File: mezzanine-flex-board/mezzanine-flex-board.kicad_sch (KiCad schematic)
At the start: 2 parts, among them J1 Mezzanine Plug, J2 Mezzanine Plug

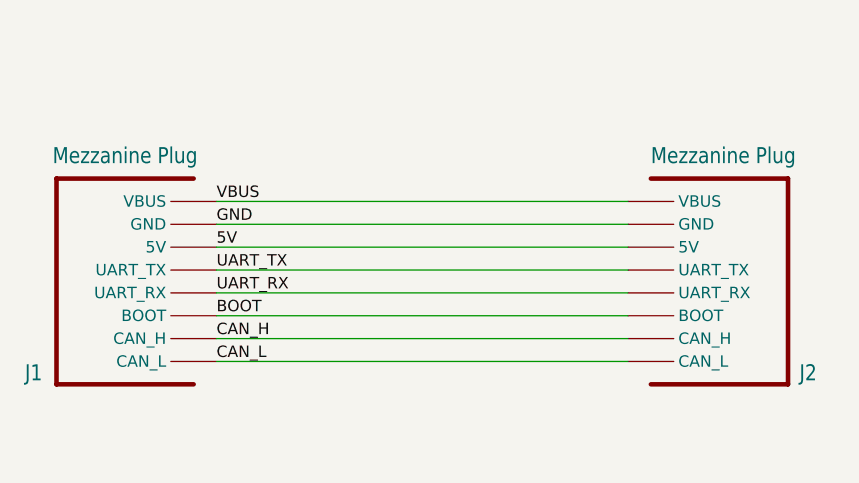
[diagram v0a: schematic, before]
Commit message: changed mezanine flex board to shorten to 14.5mm down from 19mm
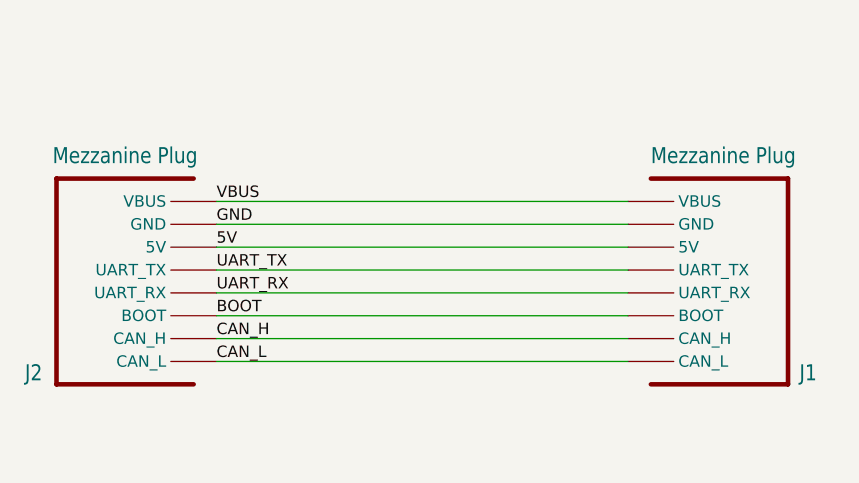
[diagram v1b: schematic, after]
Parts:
- renumbered J2 to J1, J1 to J2
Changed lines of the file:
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@@
-(kicad_sch (version 20211123) (generator eeschema)
+(kicad_sch (version 20230121) (generator eeschema)
   (paper "A4")
   (wire (pts (xy 114.3 101.6) (xy 160.02 101.6))
-    (stroke (width 0) (type default) (color 0 0 0 0))
+    (stroke (width 0) (type default))
   )
   (wire (pts (xy 114.3 99.06) (xy 160.02 99.06))
-    (stroke (width 0) (type default) (color 0 0 0 0))
+    (stroke (width 0) (type default))
   )
   (wire (pts (xy 114.3 96.52) (xy 160.02 96.52))
-    (stroke (width 0) (type default) (color 0 0 0 0))
+    (stroke (width 0) (type default))
   )
   (wire (pts (xy 114.3 91.44) (xy 160.02 91.44))
-    (stroke (width 0) (type default) (color 0 0 0 0))
+    (stroke (width 0) (type default))
   )
   (wire (pts (xy 114.3 104.14) (xy 160.02 104.14))
-    (stroke (width 0) (type default) (color 0 0 0 0))
+    (stroke (width 0) (type default))
   )
   (wire (pts (xy 114.3 88.9) (xy 160.02 88.9))
-    (stroke (width 0) (type default) (color 0 0 0 0))
+    (stroke (width 0) (type default))
   )
   (wire (pts (xy 114.3 86.36) (xy 160.02 86.36))
-    (stroke (width 0) (type default) (color 0 0 0 0))
+    (stroke (width 0) (type default))
   )
   (wire (pts (xy 114.3 93.98) (xy 160.02 93.98))
-    (stroke (width 0) (type default) (color 0 0 0 0))
+    (stroke (width 0) (type default))
   )
-  (label "BOOT" (at 114.3 99.06 0)
+  (label "BOOT" (at 114.3 99.06 0) (fields_autoplaced)
     (effects (font (size 1.27 1.27)) (justify left bottom))
   )
-  (label "5V" (at 114.3 91.44 0)
+  (label "5V" (at 114.3 91.44 0) (fields_autoplaced)
     (effects (font (size 1.27 1.27)) (justify left bottom))
   )
-  (label "CAN_H" (at 114.3 101.6 0)
+  (label "CAN_H" (at 114.3 101.6 0) (fields_autoplaced)
     (effects (font (size 1.27 1.27)) (justify left bottom))
   )
-  (label "UART_RX" (at 114.3 96.52 0)
+  (label "UART_RX" (at 114.3 96.52 0) (fields_autoplaced)
     (effects (font (size 1.27 1.27)) (justify left bottom))
   )
-  (label "GND" (at 114.3 88.9 0)
+  (label "GND" (at 114.3 88.9 0) (fields_autoplaced)
     (effects (font (size 1.27 1.27)) (justify left bottom))
   )
-  (label "CAN_L" (at 114.3 104.14 0)
+  (label "CAN_L" (at 114.3 104.14 0) (fields_autoplaced)
     (effects (font (size 1.27 1.27)) (justify left bottom))
   )
-  (label "UART_TX" (at 114.3 93.98 0)
+  (label "UART_TX" (at 114.3 93.98 0) (fields_autoplaced)
     (effects (font (size 1.27 1.27)) (justify left bottom))
   )
-  (label "VBUS" (at 114.3 86.36 0)
+  (label "VBUS" (at 114.3 86.36 0) (fields_autoplaced)
     (effects (font (size 1.27 1.27)) (justify left bottom))
   )
   (symbol (lib_id "oresat-connectors:Mezzanine Plug") (at 109.22 96.52 0) (unit 1)
-    (in_bom yes) (on_board yes)
-    (property "Reference" "J1" (id 0) (at 93.98 105.41 0)
+    (in_bom yes) (on_board yes) (dnp no)
+    (property "Reference" "J2" (at 93.98 105.41 0)
       (effects (font (size 1.778 1.5113)))
     )
-    (property "Value" "Mezzanine Plug" (id 1) (at 104.14 81.28 0)
+    (property "Value" "Mezzanine Plug" (at 104.14 81.28 0)
       (effects (font (size 1.778 1.5113)))
     )
-    (property "Footprint" "oresat-connectors:J-Molex-0547220304" (id 2) (at 109.22 96.52 0)
+    (property "Footprint" "oresat-connectors:J-Molex-0547220304" (at 109.22 96.52 0)
       (effects (font (size 1.27 1.27)) hide)
     )
-    (property "Datasheet" "" (id 3) (at 109.22 96.52 0)
+    (property "Datasheet" "" (at 109.22 96.52 0)
       (effects (font (size 1.27 1.27)) hide)
     )
@@
     (pin "P$8")
     (pin "P$9")
+    (instances
+      (project "mezzanine-flex-board"
+        (path "/73c464dd-daf4-484f-b278-4b4e429c836b"
+          (reference "J2") (unit 1)
+        )
+      )
+    )
   )
-  (symbol (lib_id "oresat-connectors:Mezzanine Plug") (at 165.1 96.52 0) (mirror y) (unit 1)
-    (in_bom yes) (on_board yes)
-    (property "Reference" "J2" (id 0) (at 179.07 105.41 0)
+  (symbol (lib_name "Mezzanine Plug_1") (lib_id "oresat-connectors:Mezzanine Plug") (at 165.1 96.52 0) (mirror y) (unit 1)
+    (in_bom yes) (on_board yes) (dnp no)
+    (property "Reference" "J1" (at 179.07 105.41 0)
       (effects (font (size 1.778 1.5113)) (justify right))
     )
-    (property "Value" "Mezzanine Plug" (id 1) (at 162.56 81.28 0)
+    (property "Value" "Mezzanine Plug" (at 162.56 81.28 0)
       (effects (font (size 1.778 1.5113)) (justify right))
     )
-    (property "Footprint" "oresat-connectors:J-Molex-0547220304" (id 2) (at 165.1 96.52 0)
+    (property "Footprint" "oresat-connectors:J-Molex-0547220304" (at 165.1 96.52 0)
       (effects (font (size 1.27 1.27)) hide)
     )
-    (property "Datasheet" "" (id 3) (at 165.1 96.52 0)
+    (property "Datasheet" "" (at 165.1 96.52 0)
       (effects (font (size 1.27 1.27)) hide)
     )
@@
     (pin "P$8")
     (pin "P$9")
+    (instances
+      (project "mezzanine-flex-board"
+        (path "/73c464dd-daf4-484f-b278-4b4e429c836b"
+          (reference "J1") (unit 1)
+        )
+      )
+    )
   )
   (sheet_instances
     (path "/" (page "1"))
   )
-  (symbol_instances
-    (path "/4513463b-8768-42d7-8671-2b20febc8418"
-      (reference "J1") (unit 1) (value "Mezzanine Plug") (footprint "oresat-connectors:J-Molex-0547220304")
-    )
-    (path "/a5af1dd9-2557-4155-9ffb-72b502d7a6a2"
-      (reference "J2") (unit 1) (value "Mezzanine Plug") (footprint "oresat-connectors:J-Molex-0547220304")
-    )
-  )
 )

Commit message: RW Flex board for Mezzanine connectors v1.2
This board is for RW board v8.0 and RW card v1.0. Note specialized Makefile for flex board including stiffeners.
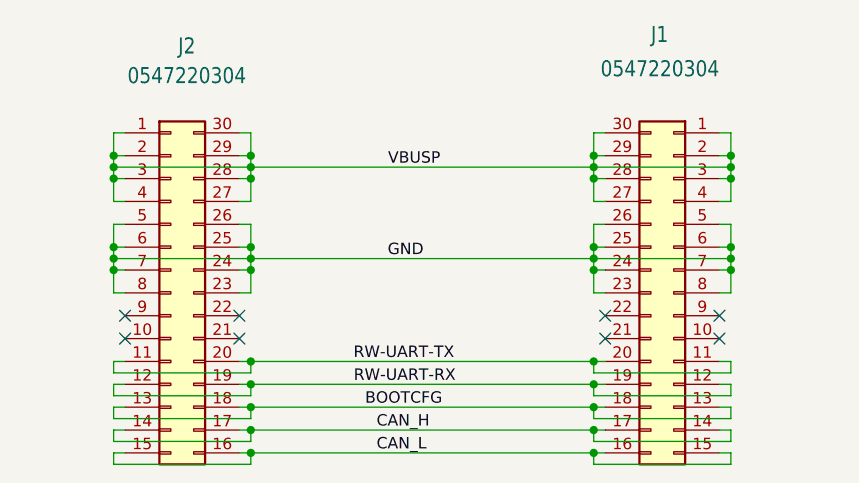
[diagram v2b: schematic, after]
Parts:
- J1, J2: value Mezzanine Plug -> 0547220304; symbol oresat-connectors:Mezzanine Plug -> Connector_Generic:Conn_02x15_Counter_Clockwise; DIS (none) -> DigiKey; DPN (none) -> WM3915CT-ND; MFR (none) -> Molex; MPN (none) -> 0547220304
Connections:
- net CAN_H: now also J1.14 (Pin_14), J1.17 (Pin_17), J2.14 (Pin_14), J2.17 (Pin_17); no longer J1.P$2 (CAN_H), J1.P$29 (CAN_H), J2.P$2 (CAN_H), J2.P$29 (CAN_H)
- net CAN_L: now also J1.15 (Pin_15), J1.16 (Pin_16), J2.15 (Pin_15), J2.16 (Pin_16); no longer J1.P$1 (CAN_L), J1.P$30 (CAN_L), J2.P$1 (CAN_L), J2.P$30 (CAN_L)
- net GND: now also J1.23 (Pin_23), J1.24 (Pin_24), J1.25 (Pin_25), J1.26 (Pin_26), J1.5 (Pin_5), J1.6 (Pin_6), J1.7 (Pin_7), J1.8 (Pin_8), J2.23 (Pin_23), J2.24 (Pin_24), J2.25 (Pin_25), J2.26 (Pin_26), J2.5 (Pin_5), J2.6 (Pin_6), J2.7 (Pin_7), J2.8 (Pin_8); no longer J1.P$10 (GND), J1.P$11 (GND), J1.P$20 (GND), J1.P$21 (GND), J1.P$22 (GND), J1.P$23 (GND), J1.P$8 (GND), J1.P$9 (GND), J2.P$10 (GND), J2.P$11 (GND), J2.P$20 (GND), J2.P$21 (GND), J2.P$22 (GND), J2.P$23 (GND), J2.P$8 (GND), J2.P$9 (GND)
- removed net 5V: J1.P$24 (5V), J1.P$25 (5V), J1.P$6 (5V), J1.P$7 (5V), J2.P$24 (5V), J2.P$25 (5V), J2.P$6 (5V), J2.P$7 (5V)
- removed net BOOT: J1.P$28 (BOOT), J1.P$3 (BOOT), J2.P$28 (BOOT), J2.P$3 (BOOT)
- removed net UART_RX: J1.P$27 (UART_RX), J1.P$4 (UART_RX), J2.P$27 (UART_RX), J2.P$4 (UART_RX)
- removed net UART_TX: J1.P$26 (UART_TX), J1.P$5 (UART_TX), J2.P$26 (UART_TX), J2.P$5 (UART_TX)
- removed net VBUS: J1.P$12 (VBUS), J1.P$13 (VBUS), J1.P$14 (VBUS), J1.P$15 (VBUS), J1.P$16 (VBUS), J1.P$17 (VBUS), J1.P$18 (VBUS), J1.P$19 (VBUS), J2.P$12 (VBUS), J2.P$13 (VBUS), J2.P$14 (VBUS), J2.P$15 (VBUS), J2.P$16 (VBUS), J2.P$17 (VBUS), J2.P$18 (VBUS), J2.P$19 (VBUS)
- new net BOOTCFG: J1.13 (Pin_13), J1.18 (Pin_18), J2.13 (Pin_13), J2.18 (Pin_18)
- new net RW-UART-RX: J1.12 (Pin_12), J1.19 (Pin_19), J2.12 (Pin_12), J2.19 (Pin_19)
- new net RW-UART-TX: J1.11 (Pin_11), J1.20 (Pin_20), J2.11 (Pin_11), J2.20 (Pin_20)
- new net VBUSP: J1.1 (Pin_1), J1.2 (Pin_2), J1.27 (Pin_27), J1.28 (Pin_28), J1.29 (Pin_29), J1.3 (Pin_3), J1.30 (Pin_30), J1.4 (Pin_4), J2.1 (Pin_1), J2.2 (Pin_2), J2.27 (Pin_27), J2.28 (Pin_28), J2.29 (Pin_29), J2.3 (Pin_3), J2.30 (Pin_30), J2.4 (Pin_4)
- no-connect marks 0 -> 8
